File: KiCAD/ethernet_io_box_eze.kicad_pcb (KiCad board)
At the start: 2 copper layers, 108 x 107.5 mm, 104 parts, among them J201 Screw_Terminal_01x02, J301 Screw_Terminal_01x03, J302 Screw_Terminal_01x03, J303 Screw_Terminal_01x03, J304 Screw_Terminal_01x03, J401 Screw_Terminal_01x04, J501 AVR-JTAG-10, J502 AVR-ISP-6, J6001 Wuerth_7499010121A, J701 Screw_Terminal_01x02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

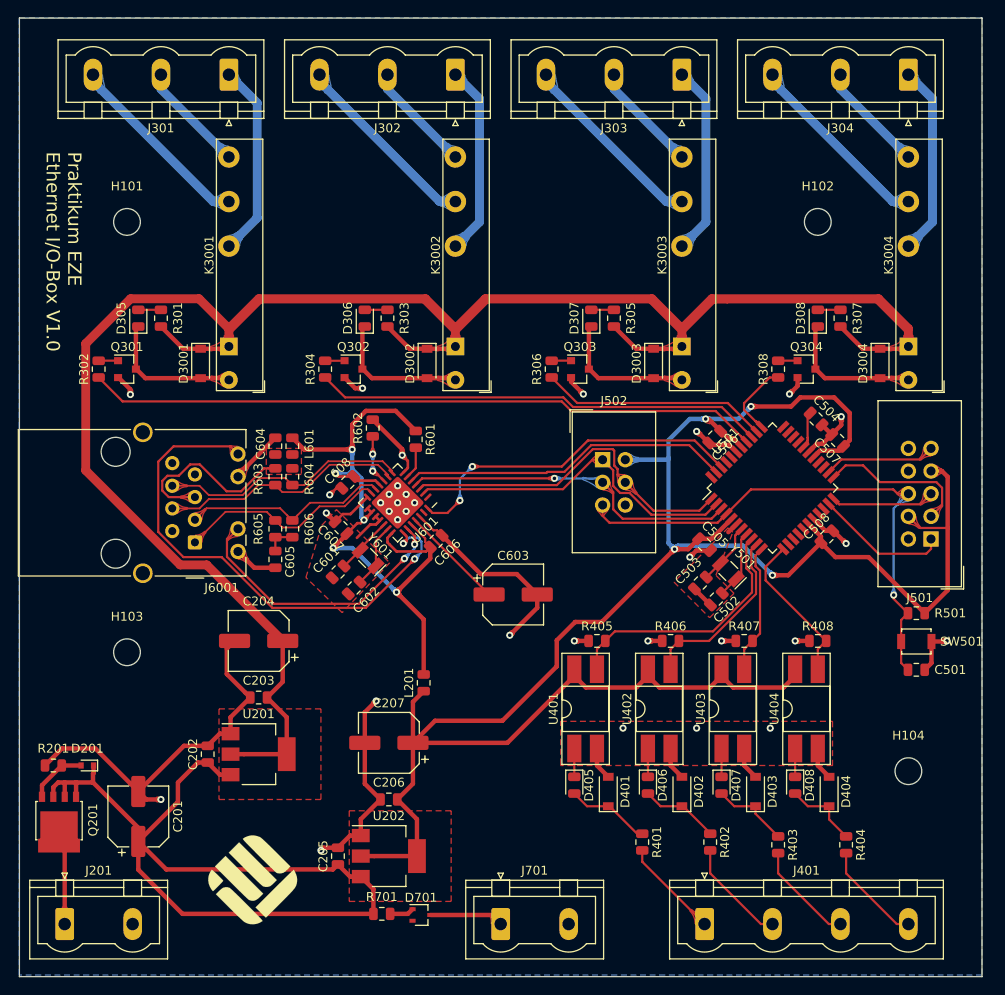
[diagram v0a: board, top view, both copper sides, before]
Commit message: Added fiducials, ignoring netlist
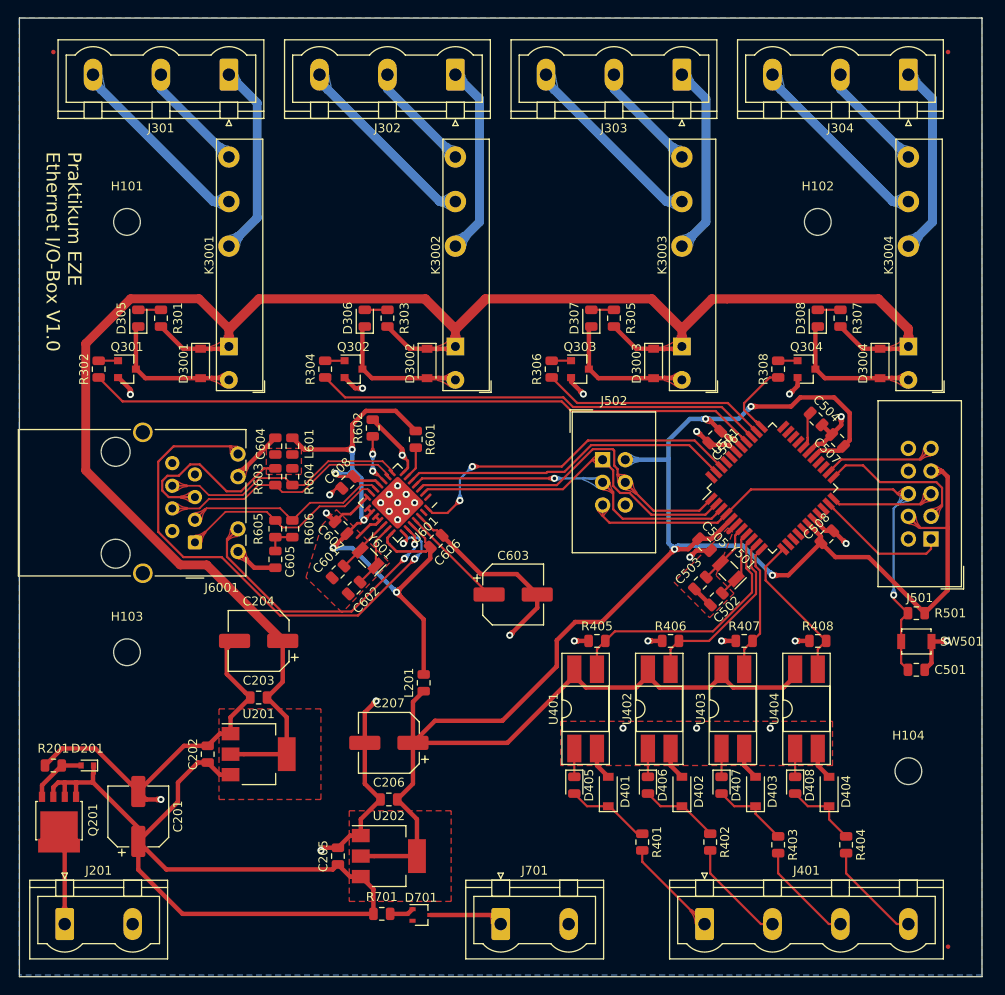
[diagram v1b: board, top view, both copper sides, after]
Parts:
- removed ?: , Logo_FH_Muenster:Logo_FH_Muenster_50mm_Silk
- removed ?: , Logo_FH_Muenster:Logo_FH_Muenster_Square_10mm_Silk
- added FID101: Fiducial, Fiducial:Fiducial_0.5mm_Mask1mm, F.Cu at (62.2, 30.5)
- added FID102: Fiducial, Fiducial:Fiducial_0.5mm_Mask1mm, F.Cu at (162.6, 30.5)
- added FID103: Fiducial, Fiducial:Fiducial_0.5mm_Mask1mm, F.Cu at (162.6, 130.8)
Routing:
- net LEDB: track 58.7 -> 59.4 mm
- net LEDA: track 32.6 -> 33.3 mm

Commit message: Moved reset button. Added the FH-Muenster logo on silk-screen.
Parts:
- added ?: , Logo_FH_Muenster:Logo_FH_Muenster_30mm_Silk, F.Cu at (91.4, 129.5)
- moved C501 3.59 mm to (156.5, 102.3)
- moved SW501 3.59 mm to (156.5, 99.1)
- moved R501 3.59 mm to (156.5, 95.9)
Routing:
- net +3V3: track 241.1 -> 246.9 mm
- net ~RESET: track 59.3 -> 61.6 mm

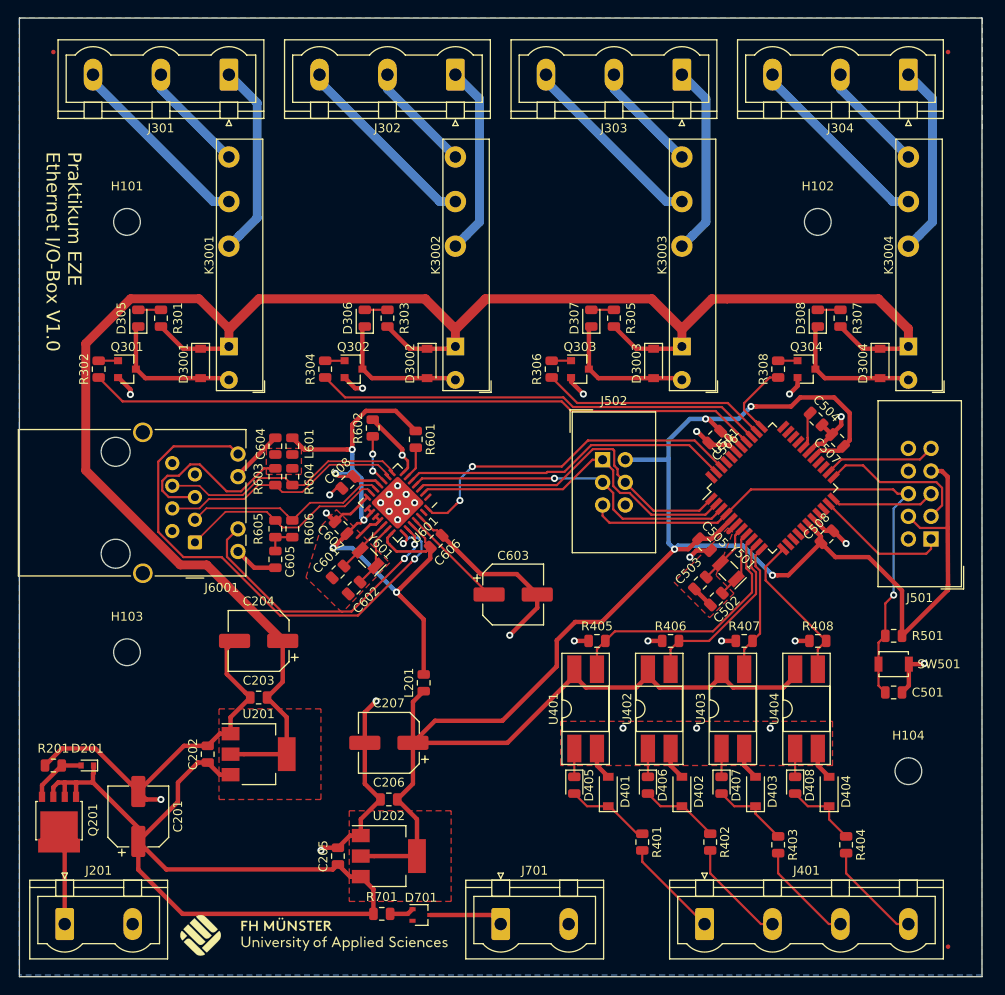
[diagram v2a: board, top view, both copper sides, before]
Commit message: Added teardrops. Changes clearance setting in board setup from 1 mm to 5 5mm for 230 net.
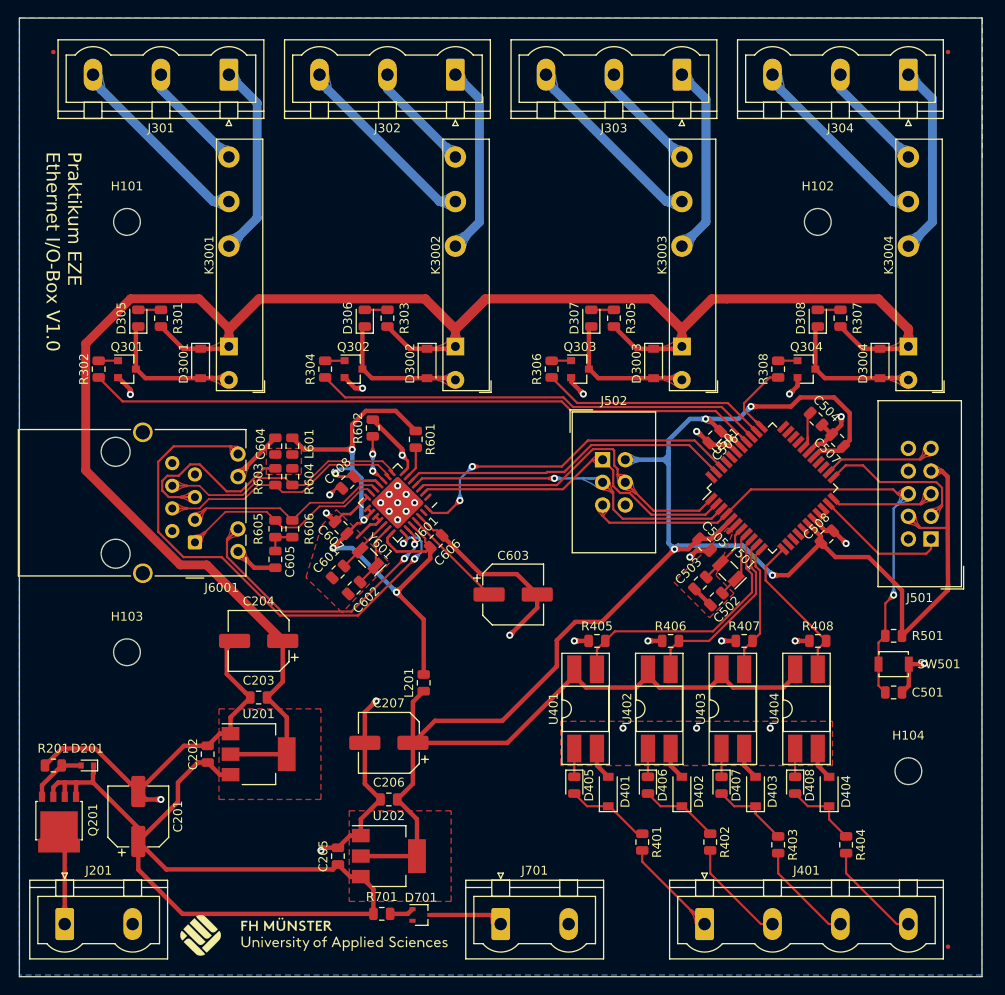
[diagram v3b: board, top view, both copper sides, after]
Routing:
- net +3V3: track 246.9 -> 248.7 mm
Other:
- net class 230V: clearance 1 -> 5
